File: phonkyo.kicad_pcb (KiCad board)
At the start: 2 copper layers, 65 x 30 mm, 37 parts, among them J1 GPIO, J2 LineOutJack, J4 RIJack, U1 CAT24C256, U2 PCM5102A, U3 XC6206P332MR

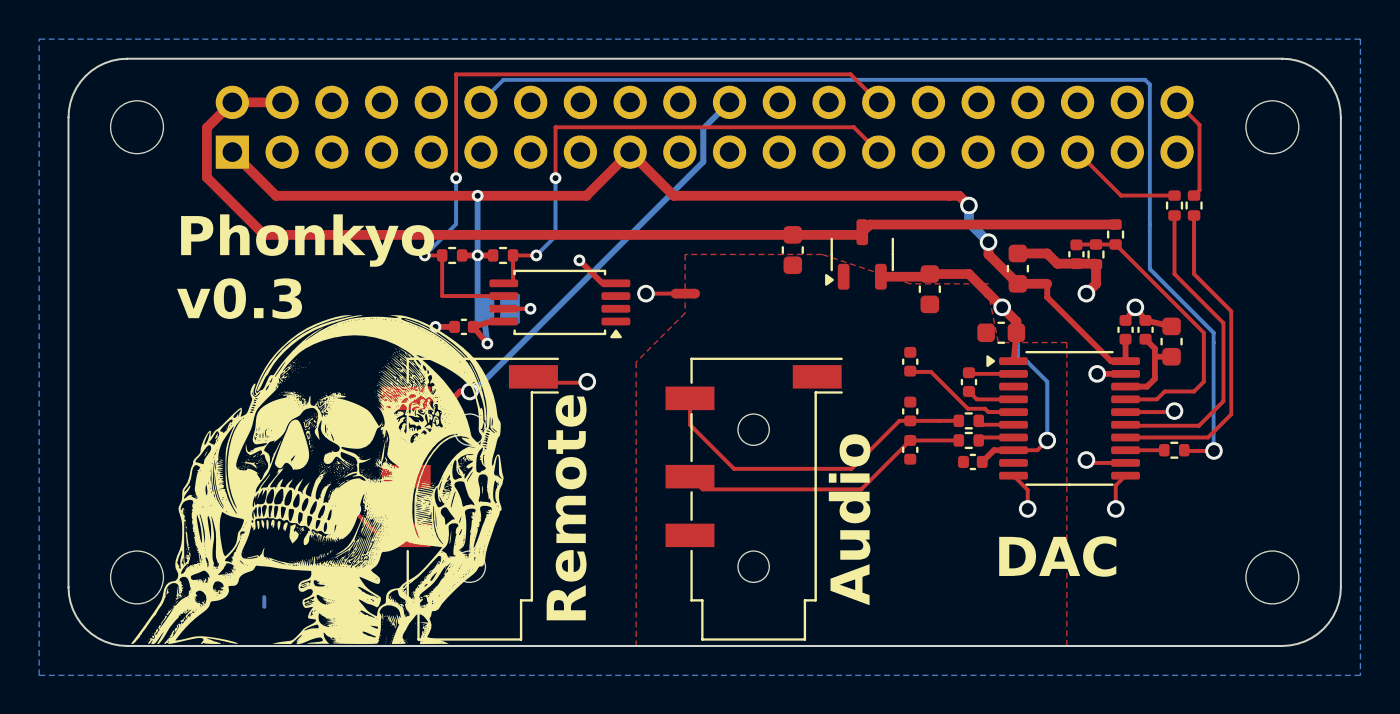
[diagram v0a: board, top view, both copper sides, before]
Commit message: pcb: move BCK to F.Cu; ESD clamp and series resistor on RI; PWR_FLAGs
BCK (GPIO18) no longer runs 55 mm on B.Cu. Its top-edge run now sits on
F.Cu above the header (y 70.55), over an unbroken B.Cu ground. It drops
through the header gap at x 155.3 to one via, then takes the existing
short B.Cu path to R9. BCK on B.Cu: 54.8 -> 15.1 mm. Total B.Cu track:
102.5 -> 64.1 mm. The GND pour stays one piece and grows 1715 -> 1734 mm2.

To make room, ID_SCL drops through the header gap east of pin 12, and the
+3V3 hop to the EEPROM comes from a rail via at x 123.6. Their B.Cu
segments stay parallel and do not cross.

RI protection: GPIO25 is split where it passes between the +3V3 and +5V
rails. J4's tip now reaches the Pi through R12 (100 R, C25076), with D1
(ESD5Z5.0T1G, C82044) clamping the jack side to GND. The 5 V standoff
leaves a 5 V receiver unclipped. 100 R keeps the transmit level safe
against the receiver's unknown pull-down and limits current into the GPIO
compared with the direct connection. There was no room at the jack
itself: the skull logo and the jack body surround it.

Schematic: R12 and D1 at J4, PWR_FLAGs on +5V, +3V3, GND and GNDA (ERC's
4 power_pin_not_driven errors are gone), and the leftover DNP flag on
JP1's +3V3 symbol is cleared.

DRC with parity: 0 unconnected, 0 parity, library warnings only. ERC: no
errors. Production files are regenerated: 30 placed parts.

Co-Authored-By: Claude Opus 5.5 <noreply@anthropic.com>
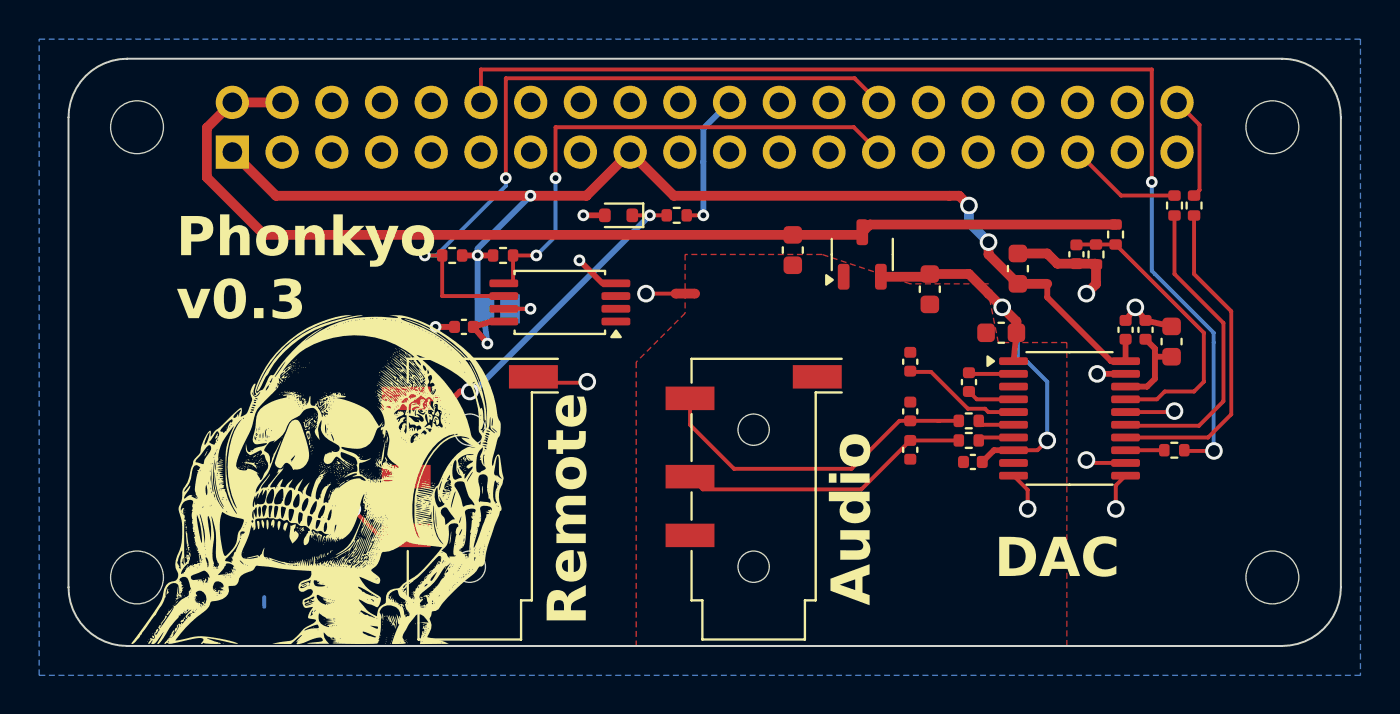
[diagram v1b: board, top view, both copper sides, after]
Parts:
- added D1: ESD5Z5.0, Diode_SMD:D_SOD-523, F.Cu at (128.1, 78.0)
- added R12: 100, Resistor_SMD:R_0402_1005Metric, F.Cu at (131.1, 78.0)
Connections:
- J4 pad T: /GPIO25 -> Net-(D1-K)
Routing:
- net Net-(D1-K): track 0.00 -> 18.1 mm, vias 0 -> 2
- net /GPIO25: track 23.8 -> 7.17 mm
- net /GPIO18/PCM.CLK: track 56.4 -> 58.3 mm, vias 1 -> 2
- net /ID_SCL: track 37.6 -> 36.1 mm
- net +3V3: track 64.4 -> 65.5 mm
- net GND: track 32.4 -> 33.5 mm, vias 12 -> 13
